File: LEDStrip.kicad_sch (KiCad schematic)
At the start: 4 parts, among them J801 WAGO-2065, J802 WAGO-2065, J803 WAGO-2065, U801 74AHC1G125

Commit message: Update parts
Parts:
- J801, J802, J803: value WAGO-2065 -> WAGO 2065-100; Manufacturer (none) -> WAGO; Product (none) -> 2065-100/998-403
- U801: footprint Package_TO_SOT_SMD:SOT-23-5 -> V2_Package_TO_SOT_SMD:SOT-23-5; Manufacturer (none) -> Texas Instruments; Mouser (none) -> 595-SN74AHC1G125DBVR; Product (none) -> SN74AHC1G125DBVR
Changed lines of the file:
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@@
 	)
 	(symbol
-		(lib_id "power:GND")
+		(lib_id "V2_power:GND")
 		(at 170.18 106.68 270)
 		(unit 1)
@@
 		(at 175.26 106.68 0)
 		(unit 1)
-		(exclude_from_sim yes)
+		(exclude_from_sim no)
 		(in_bom yes)
 		(on_board yes)
@@
 			)
 		)
-		(property "Value" "WAGO-2065"
+		(property "Value" "WAGO 2065-100"
 			(at 175.26 113.03 0)
 			(effects
@@
 					(size 1.27 1.27)
 				)
-				(hide yes)
 			)
 		)
@@
 		)
 		(property "Description" ""
+			(at 175.26 106.68 0)
+			(effects
+				(font
+					(size 1.27 1.27)
+				)
+				(hide yes)
+			)
+		)
+		(property "Manufacturer" "WAGO"
+			(at 175.26 119.888 0)
+			(effects
+				(font
+					(size 1.27 1.27)
+				)
+				(hide yes)
+			)
+		)
+		(property "Product" "2065-100/998-403"
+			(at 175.26 123.19 0)
+			(effects
+				(font
+					(size 1.27 1.27)
+				)
+				(hide yes)
+			)
+		)
+		(property "Sim.Pin" ""
 			(at 175.26 106.68 0)
 			(effects
@@
 	)
 	(symbol
-		(lib_id "power:+5V")
+		(lib_id "V2_power:+5V")
 		(at 170.18 101.6 90)
 		(unit 1)
@@
 		(at 175.26 101.6 0)
 		(unit 1)
-		(exclude_from_sim yes)
+		(exclude_from_sim no)
 		(in_bom yes)
 		(on_board yes)
@@
 			)
 		)
-		(property "Value" "WAGO-2065"
+		(property "Value" "WAGO 2065-100"
 			(at 175.26 107.95 0)
 			(effects
@@
 					(size 1.27 1.27)
 				)
-				(hide yes)
 			)
 		)
@@
 		)
 		(property "Description" ""
+			(at 175.26 101.6 0)
+			(effects
+				(font
+					(size 1.27 1.27)
+				)
+				(hide yes)
+			)
+		)
+		(property "Manufacturer" "WAGO"
+			(at 175.26 114.808 0)
+			(effects
+				(font
+					(size 1.27 1.27)
+				)
+				(hide yes)
+			)
+		)
+		(property "Product" "2065-100/998-403"
+			(at 175.26 118.11 0)
+			(effects
+				(font
+					(size 1.27 1.27)
+				)
+				(hide yes)
+			)
+		)
+		(property "Sim.Pin" ""
 			(at 175.26 101.6 0)
 			(effects
@@
 	)
 	(symbol
-		(lib_id "power:+5V")
+		(lib_id "V2_power:+5V")
 		(at 139.7 104.14 0)
 		(unit 1)
@@
 	)
 	(symbol
-		(lib_id "power:GND")
+		(lib_id "V2_power:GND")
 		(at 139.7 115.57 0)
 		(unit 1)
@@
 		(at 175.26 111.76 0)
 		(unit 1)
-		(exclude_from_sim yes)
+		(exclude_from_sim no)
 		(in_bom yes)
 		(on_board yes)
@@
 			)
 		)
-		(property "Value" "WAGO-2065"
+		(property "Value" "WAGO 2065-100"
 			(at 175.26 118.11 0)
 			(effects
@@
 					(size 1.27 1.27)
 				)
-				(hide yes)
 			)
 		)
@@
 		)
 		(property "Description" ""
+			(at 175.26 111.76 0)
+			(effects
+				(font
+					(size 1.27 1.27)
+				)
+				(hide yes)
+			)
+		)
+		(property "Manufacturer" "WAGO"
+			(at 175.26 124.968 0)
+			(effects
+				(font
+					(size 1.27 1.27)
+				)
+				(hide yes)
+			)
+		)
+		(property "Product" "2065-100/998-403"
+			(at 175.26 128.27 0)
+			(effects
+				(font
+					(size 1.27 1.27)
+				)
+				(hide yes)
+			)
+		)
+		(property "Sim.Pin" ""
 			(at 175.26 111.76 0)
 			(effects
@@
 			)
 		)
-		(property "Footprint" "Package_TO_SOT_SMD:SOT-23-5"
+		(property "Footprint" "V2_Package_TO_SOT_SMD:SOT-23-5"
 			(at 138.43 111.76 0)
 			(effects
@@
 			(effects
 				(font
+					(size 1.27 1.27)
+				)
+				(hide yes)
+			)
+		)
+		(property "Mouser" "595-SN74AHC1G125DBVR"
+			(at 138.43 138.43 0)
+			(effects
+				(font
+					(size 1.27 1.27)
+				)
+				(hide yes)
+			)
+		)
+		(property "Sim.Pin" ""
+			(at 138.43 111.76 0)
+			(effects
+				(font
+					(size 1.27 1.27)
+				)
+				(hide yes)
+			)
+		)
+		(property "Product" "SN74AHC1G125DBVR"
+			(at 138.43 137.16 0)
+			(effects
+				(font
+					(size 1.27 1.27)
+				)
+				(hide yes)
+			)
+		)
+		(property "Manufacturer" "Texas Instruments"
+			(at 138.43 134.62 0)
+			(effects
+				(font

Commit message: Replace diode
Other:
- title: LED Strip -> V2 drum

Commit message: Update
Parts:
- J801, J802, J803: Id (none) -> WAGO:${SYMBOL_NAME}; Rating (none) -> 9A
- U801: Id (none) -> 74xGxx:${SYMBOL_NAME}; Rating (none) -> 8mA
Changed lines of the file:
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@@
 	(title_block
 		(title "V2 drum")
-		(date "2026-03-30")
+		(date "2026-04-14")
 		(rev "2026-03-30")
 		(company "Versio Duo")
+		(comment 1 "Percussion Controller")
 	)
 	(junction
@@
 		(in_pos_files yes)
 		(dnp no)
-		(property "Reference" "#PWR803"
+		(property "Reference" "#PWR0804"
 			(at 163.83 106.68 0)
 			(hide yes)
@@
 			(project "drum"
 				(path "/6c8448b4-b04d-47e1-934e-e40cbe27a7be/48b625e4-a08e-4317-bdf1-f52549e397dd"
-					(reference "#PWR803")
+					(reference "#PWR0804")
 					(unit 1)
 				)
@@
 			)
 		)
+		(property "Id" "WAGO:${SYMBOL_NAME}"
+			(at 175.26 114.3 0)
+			(hide yes)
+			(show_name no)
+			(do_not_autoplace no)
+			(effects
+				(font
+					(size 1.27 1.27)
+				)
+			)
+		)
+		(property "Rating" "9A"
+			(at 175.26 124.46 0)
+			(hide yes)
+			(show_name no)
+			(do_not_autoplace no)
+			(effects
+				(font
+					(size 1.27 1.27)
+				)
+			)
+		)
 		(pin "1"
 		)
@@
 		(in_pos_files yes)
 		(dnp no)
-		(property "Reference" "#PWR801"
+		(property "Reference" "#PWR0803"
 			(at 173.99 101.6 0)
 			(hide yes)
@@
 			(project "drum"
 				(path "/6c8448b4-b04d-47e1-934e-e40cbe27a7be/48b625e4-a08e-4317-bdf1-f52549e397dd"
-					(reference "#PWR801")
+					(reference "#PWR0803")
 					(unit 1)
 				)
@@
 			)
 		)
+		(property "Id" "WAGO:${SYMBOL_NAME}"
+			(at 175.26 109.22 0)
+			(hide yes)
+			(show_name no)
+			(do_not_autoplace no)
+			(effects
+				(font
+					(size 1.27 1.27)
+				)
+			)
+		)
+		(property "Rating" "9A"
+			(at 175.26 119.38 0)
+			(hide yes)
+			(show_name no)
+			(do_not_autoplace no)
+			(effects
+				(font
+					(size 1.27 1.27)
+				)
+			)
+		)
 		(pin "1"
 		)
@@
 		(in_pos_files yes)
 		(dnp no)
-		(property "Reference" "#PWR802"
+		(property "Reference" "#PWR0801"
 			(at 139.7 107.95 0)
 			(hide yes)
@@
 			(project "drum"
 				(path "/6c8448b4-b04d-47e1-934e-e40cbe27a7be/48b625e4-a08e-4317-bdf1-f52549e397dd"
-					(reference "#PWR802")
+					(reference "#PWR0801")
 					(unit 1)
 				)
@@
 		(in_pos_files yes)
 		(dnp no)
-		(property "Reference" "#PWR804"
+		(property "Reference" "#PWR0802"
 			(at 139.7 121.92 0)
 			(hide yes)
@@
 			(project "drum"
 				(path "/6c8448b4-b04d-47e1-934e-e40cbe27a7be/48b625e4-a08e-4317-bdf1-f52549e397dd"
-					(reference "#PWR804")
+					(reference "#PWR0802")
 					(unit 1)
 				)
@@
 			)
 		)
+		(property "Id" "WAGO:${SYMBOL_NAME}"
+			(at 175.26 119.38 0)
+			(hide yes)
+			(show_name no)
+			(do_not_autoplace no)
+			(effects
+				(font
+					(size 1.27 1.27)
+				)
+			)
+		)
+		(property "Rating" "9A"
+			(at 175.26 129.54 0)
+			(hide yes)
+			(show_name no)
+			(do_not_autoplace no)
+			(effects
+				(font
+					(size 1.27 1.27)
+				)
+			)
+		)
 		(pin "1"
 		)
@@
 			(hide yes)
 			(show_name no)
+			(do_not_autoplace no)
+			(effects
+				(font
+					(size 1.27 1.27)
+				)
+			)
+		)
+		(property "Id" "74xGxx:${SYMBOL_NAME}"
+			(at 138.43 124.46 0)
+			(hide yes)
+			(show_name no)
+			(do_not_autoplace no)
+			(effects
+				(font
+					(size 1.27 1.27)
+				)
+			)
+		)
+		(property "Rating" "8mA"
+			(at 138.43 142.24 0)
+			(hide yes)
+			(show_name no)

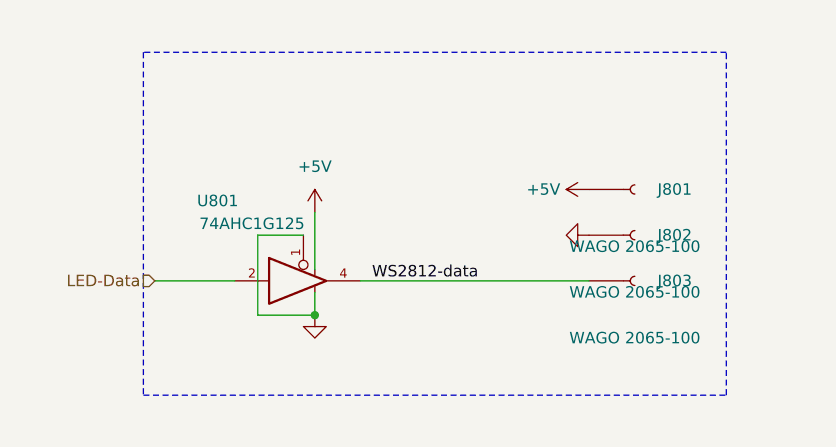
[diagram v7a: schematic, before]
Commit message: Switch to 6 layer
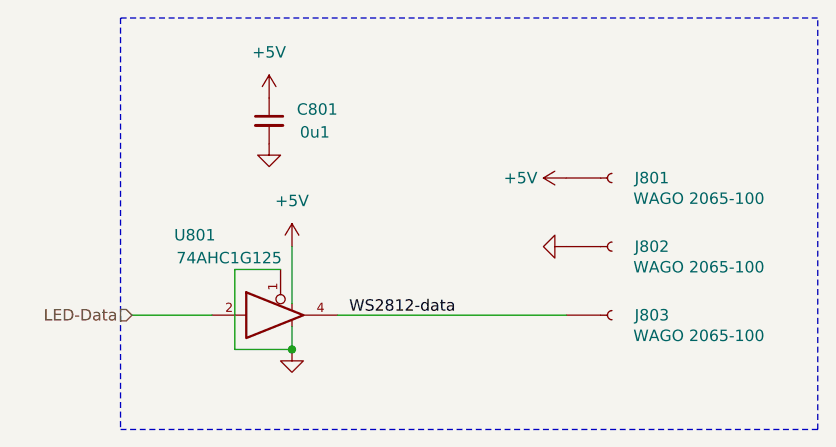
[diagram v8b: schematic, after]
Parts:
- added C801: 0u1, V2_Capacitor_SMD:C_1608, symbol V2_Capacitor:1608_0u1
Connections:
- net +5V: now also C801.1
- net GND: now also C801.2
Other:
- moved on the sheet: J801, J802, J803, U801
